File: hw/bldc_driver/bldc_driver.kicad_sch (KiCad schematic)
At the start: 25 parts, among them U1 CH32V30xRxTx, U14 SN65HVD230, U8 TPS54202DDC

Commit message: feat: add CNCs
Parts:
- removed R2: 300 ohm, Resistor_SMD:R_0603_1608Metric_Pad0.98x0.95mm_HandSolder, symbol #inventree:RC0603FR-07300RL
- added D15, D16, D17: KT-0603W, LED_SMD:LED_0603_1608Metric_Pad1.05x0.95mm_HandSolder, symbol Device:LED
- added J1: 430450412, Connector_Molex:Molex_Micro-Fit_3.0_43045-0412_2x02_P3.00mm_Vertical, symbol Connector_Generic:Conn_02x02_Odd_Even
- added J2: B4B-EH-A(LF)(SN), Connector_JST:JST_EH_B4B-EH-A_1x04_P2.50mm_Vertical, symbol Connector_Generic:Conn_01x04
- added J4: 1733583, TerminalBlock_Phoenix:TerminalBlock_Phoenix_MKDS-1,5-3-5.08_1x03_P5.08mm_Horizontal, symbol Connector:Screw_Terminal_01x03
- added R2, R36, R37, R6: 100 Ohm, Resistor_SMD:R_0603_1608Metric_Pad0.98x0.95mm_HandSolder, symbol Device:R
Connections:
- net +3V3: now also J2.4 (Pin_4)
- net +VDC: now also J1.1 (Pin_1)
- net GND: now also J2.1 (Pin_1), R2.1, R36.2, R37.2, R6.2
- net GNDPWR: now also J1.3 (Pin_3)
- net Motor/MOTOR_U: now also J4.1 (Pin_1)
- net Motor/MOTOR_V: now also J4.2 (Pin_2)
- net Motor/MOTOR_W: now also J4.3 (Pin_3)
- net Motor/PH_U_HI: now also U1.37 (PC6)
- net Motor/PH_U_LO: now also U1.38 (PC7)
- net Motor/PH_V_HI: now also U1.39 (PC8)
- net Motor/PH_V_LO: now also U1.40 (PC9)
- net Motor/PH_W_HI: now also U1.51 (PC10)
- net Motor/PH_W_LO: now also U1.52 (PC11)
- net Motor/SHUNT_CURR_P: now also U1.11 (PC3)
- net Motor/U_ADC_P: now also U1.8 (PC0)
- net Motor/V_ADC_P: now also U1.9 (PC1)
- net Motor/W_ADC_P: now also U1.10 (PC2)
- net at U1.34 (PB13): now also D15.2 (A)
- net at U1.35 (PB14): now also D16.2 (A)
- net at U1.36 (PB15): now also D17.2 (A)
- net at U1.46 (SWDIO): now also J2.3 (Pin_3)
- net at U1.49 (SWCLK): now also J2.2 (Pin_2)
- net at D1.1 (K): now also R2.2
- net CAN_L: now reaches U14.6 (CANL)
- net CAN_L: now also J1.4 (Pin_4)
- net CAN_H: now reaches U14.7 (CANH)
- net CAN_H: now also J1.2 (Pin_2)
- new net: D17.1 (K), R37.1
- new net: D15.1 (K), R6.1
- new net: D16.1 (K), R36.1
- no-connect marks 0 -> 6
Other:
- moved on the sheet: C1, C2, C3, C39, C4, C5, C6, C7, C8, C9, D1, D2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

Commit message: feat: start PCB
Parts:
- added F1: BSMD1206C-2200T, Fuse:Fuse_1206_3216Metric_Pad1.42x1.75mm_HandSolder, symbol Device:Fuse
- added J3: B4B-EH-A(LF)(SN), Connector_JST:JST_EH_B4B-EH-A_1x04_P2.50mm_Vertical, symbol Connector_Generic:Conn_01x04
- added TP6, TP7, TP8, TP9: TestPoint_Flag, TestPoint:TestPoint_Plated_Hole_D2.0mm, symbol Connector:TestPoint_Flag
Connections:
- net +3V3: now also J3.4 (Pin_4)
- net +VDC: now also F1.1; no longer J1.1 (Pin_1)
- net GND: now also J3.1 (Pin_1)
- net Motor/MOTOR_U: now also TP9.1
- net Motor/MOTOR_V: now also TP8.1
- net Motor/MOTOR_W: now also TP7.1
- net USART3_TX: now reaches U1.29 (PB10)
- net USART3_TX: now also J3.3 (Pin_3)
- net USART3_RX: now reaches U1.30 (PB11)
- net USART3_RX: now also J3.2 (Pin_2)
- new net: F1.2, J1.1 (Pin_1), TP6.1
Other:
- moved on the sheet: D1, J2, R2

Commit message: bldc: start placement
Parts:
- added C40: 0.1 µF, Capacitor_SMD:C_0805_2012Metric_Pad1.18x1.45mm_HandSolder, symbol #inventree:CL21B104KBCNNNC
- added C41, C42: 10 pF, Capacitor_SMD:C_0805_2012Metric_Pad1.18x1.45mm_HandSolder, symbol #inventree:CL21C100CBANNNC
- added R38, R39, R40: 4.7 kohm, Resistor_SMD:R_0603_1608Metric_Pad0.98x0.95mm_HandSolder, symbol #inventree:RC0603FR-074K7L
- added Y1: Crystal_GND24, Crystal:Crystal_SMD_3225-4Pin_3.2x2.5mm_HandSoldering, symbol Device:Crystal_GND24
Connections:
- net +3V3: now also R38.1, R39.1
- net GND: now also C40.2, C41.2, C42.2, R40.2, Y1.2, Y1.4
- net Motor/MOTOR_U: now also J4.3 (Pin_3); no longer J4.1 (Pin_1)
- net Motor/MOTOR_W: now also J4.1 (Pin_1); no longer J4.3 (Pin_3)
- net SWDIO: now reaches J2.3 (Pin_3), U1.46 (SWDIO)
- net SWCLK: now reaches J2.2 (Pin_2), U1.49 (SWCLK)
- net at U1.5 (OSC_IN): now also C41.1, Y1.3
- net at U1.6 (OSC_OUT): now also C42.1, Y1.1
- net at U1.60 (BOOT0): now also R39.2, R40.1
- net at U1.7 (~{RST}): now also C40.1, R38.2
- no-connect marks 6 -> 35
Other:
- note added: "RST BTN"
- moved on the sheet: C1, C2, C3, C4, C8, C9, R1, U1

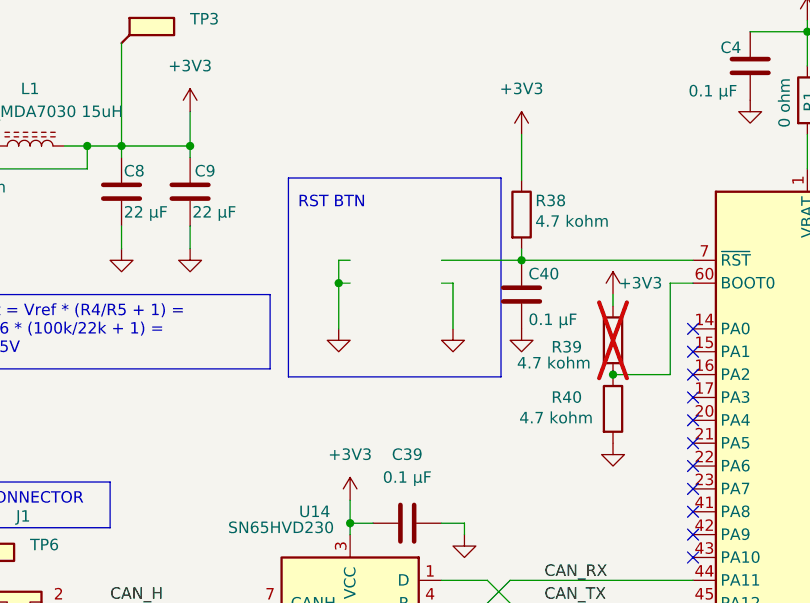
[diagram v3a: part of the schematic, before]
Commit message: bldc: placement mostly done
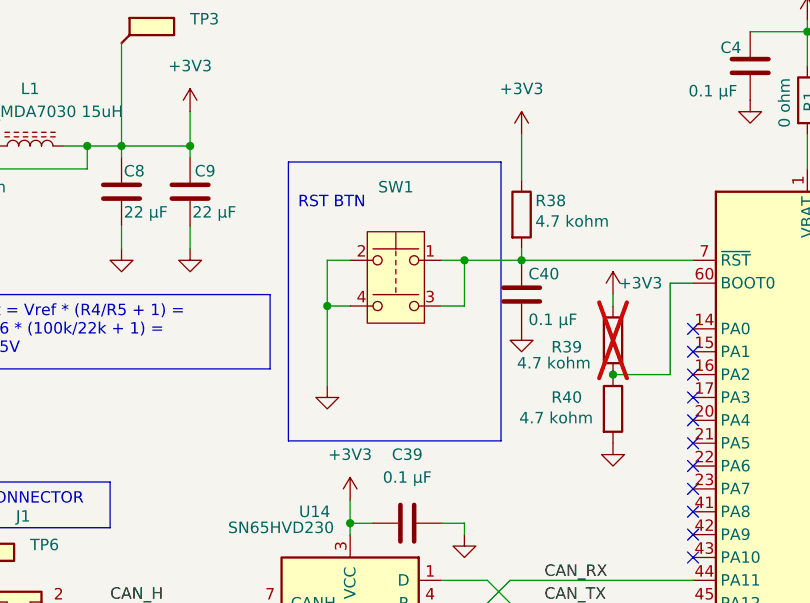
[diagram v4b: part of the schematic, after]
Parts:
- added SW1: BTSA-N-P-1, Button_Switch_THT:SW_PUSH_6mm_H8mm, symbol Switch:SW_Push_Dual
- R3: footprint Resistor_SMD:R_0201_0603Metric_Pad0.64x0.40mm_HandSolder -> Resistor_SMD:R_0603_1608Metric_Pad0.98x0.95mm_HandSolder
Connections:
- net GND: now also SW1.2, SW1.4
- net at C40.1, R38.2, U1.7 (~{RST}): now also SW1.1, SW1.3

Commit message: before reroute
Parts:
- removed C1, C2, C3, C4: 0.1 µF, Capacitor_SMD:C_0805_2012Metric_Pad1.18x1.45mm_HandSolder, symbol #inventree:CL21B104KBCNNNC
- removed U1: CH32V30xRxTx, Package_QFP:LQFP-64_10x10mm_P0.5mm, symbol MCU_WCH_CH32V3:CH32V30xRxTx
- added C55: 10 µF, Capacitor_SMD:C_0805_2012Metric_Pad1.18x1.45mm_HandSolder, symbol #inventree:CL21A106KOQNNNE
- added C56, C57, C58, C60: 0.1 µF, Capacitor_SMD:C_0805_2012Metric_Pad1.18x1.45mm_HandSolder, symbol #inventree:CL21B104KBCNNNC
- added C59: 1 µF, Capacitor_SMD:C_0805_2012Metric_Pad1.18x1.45mm_HandSolder, symbol #inventree:CL21B104KBCNNNC
- added C61: 10 nF, Capacitor_SMD:C_0805_2012Metric_Pad1.18x1.45mm_HandSolder, symbol #inventree:CL21B104KBCNNNC
- added R41, R42, R43, R44: 0 ohm, Resistor_SMD:R_0603_1608Metric_Pad0.98x0.95mm_HandSolder, symbol #inventree:RC0603FR-070RL
- added U15: STM32L431CCTx, Package_QFP:LQFP-48_7x7mm_P0.5mm, symbol MCU_ST_STM32L4:STM32L431CCTx
- added U16, U17: SN74LVC1G125DBV, Package_TO_SOT_SMD:SOT-23-5_HandSoldering, symbol 74xGxx:SN74LVC1G125DBV
- J2: value B4B-EH-A(LF)(SN) -> B6B-EH-A(LF)(SN); footprint Connector_JST:JST_EH_B4B-EH-A_1x04_P2.50mm_Vertical -> Connector_JST:JST_EH_B6B-EH-A_1x06_P2.50mm_Vertical; symbol Connector_Generic:Conn_01x04 -> Connector_Generic:Conn_01x06
- R4: footprint Resistor_SMD:R_0201_0603Metric_Pad0.64x0.40mm_HandSolder -> Resistor_SMD:R_0603_1608Metric_Pad0.98x0.95mm_HandSolder
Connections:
- net +3V3: now also J2.6 (Pin_6), C55.1, C56.2, C57.2, C58.2, C59.2, C60.2, C61.2, U15.24 (VDD), U15.36 (VDD), U15.48 (VDD), U15.9 (VDDA), U16.5 (VCC), U17.5 (VCC); no longer J2.4 (Pin_4)
- net CAN_RX: now also U14.1 (D), R42.1; no longer U14.4 (R)
- net CAN_TX: now also U14.4 (R), R41.2; no longer U14.1 (D)
- net GND: now also C41.1, C42.1, C55.2, C56.1, C57.1, C58.1, C59.1, C60.1, C61.1, U15.23 (VSS), U15.35 (VSS), U15.47 (VSS), U15.8 (VSSA), U16.1, U16.3 (GND), U17.1, U17.3 (GND); no longer C41.2, C42.2
- net Motor/MOTOR_U: now also TP7.1; no longer TP9.1
- net Motor/MOTOR_W: now also TP9.1; no longer TP7.1
- net SWCLK: now also J2.3 (Pin_3), U15.37 (PA14); no longer J2.2 (Pin_2)
- net SWDIO: now also J2.4 (Pin_4), U15.34 (PA13); no longer J2.3 (Pin_3)
- net at R1.2: now also U15.1 (VBAT)
- net at D15.2 (A): now also U15.38 (PA15)
- net at D16.2 (A): now also U15.39 (PB3)
- net at D17.2 (A): now also U15.22 (PB11)
- net at Y1.3: now also C41.2, U15.5 (PH0); no longer C41.1
- net at Y1.1: now also C42.2, U15.6 (PH1); no longer C42.1
- net at R39.2, R40.1: now also U15.44 (PH3)
- net NRESET: now reaches C40.1, R38.2, SW1.1, SW1.3
- net NRESET: now also R44.2, U15.7 (NRST)
- net USART3_RX renamed USART1_RX
- net USART1_RX: now also U16.2
- net USART3_TX renamed USART1_TX
- net USART1_TX: now also U17.4
- new net: J2.2 (Pin_2), R43.1
- new net: U15.43 (PB7), U16.4
- new net: R42.2, U15.33 (PA12)
- new net: R41.1, U15.32 (PA11)
- new net: J2.5 (Pin_5), R44.1
- new net: U15.42 (PB6), U17.2
- new net PH_U_HI: U15.29 (PA8)
- new net PH_U_LO: U15.26 (PB13)
- new net PH_V_HI: U15.30 (PA9)
- new net PH_V_LO: U15.27 (PB14)
- new net PH_W_HI: U15.31 (PA10)
- new net PH_W_LO: U15.28 (PB15)
- new net SHUNT_CURR_N: U15.17 (PA7)
- new net SHUNT_CURR_P: U15.16 (PA6)
- new net U_ADC_N: U15.11 (PA1)
- new net U_ADC_P: U15.10 (PA0)
- new net V_ADC_N: U15.13 (PA3)
- new net V_ADC_P: U15.12 (PA2)
- new net W_ADC_N: U15.15 (PA5)
- new net W_ADC_P: U15.14 (PA4)
- no-connect marks 35 -> 14
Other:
- note added: "ADC1"
- moved on the sheet: C39, C40, C41, C42, D15, D16, D17, F1, J1, J3, J4, R1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

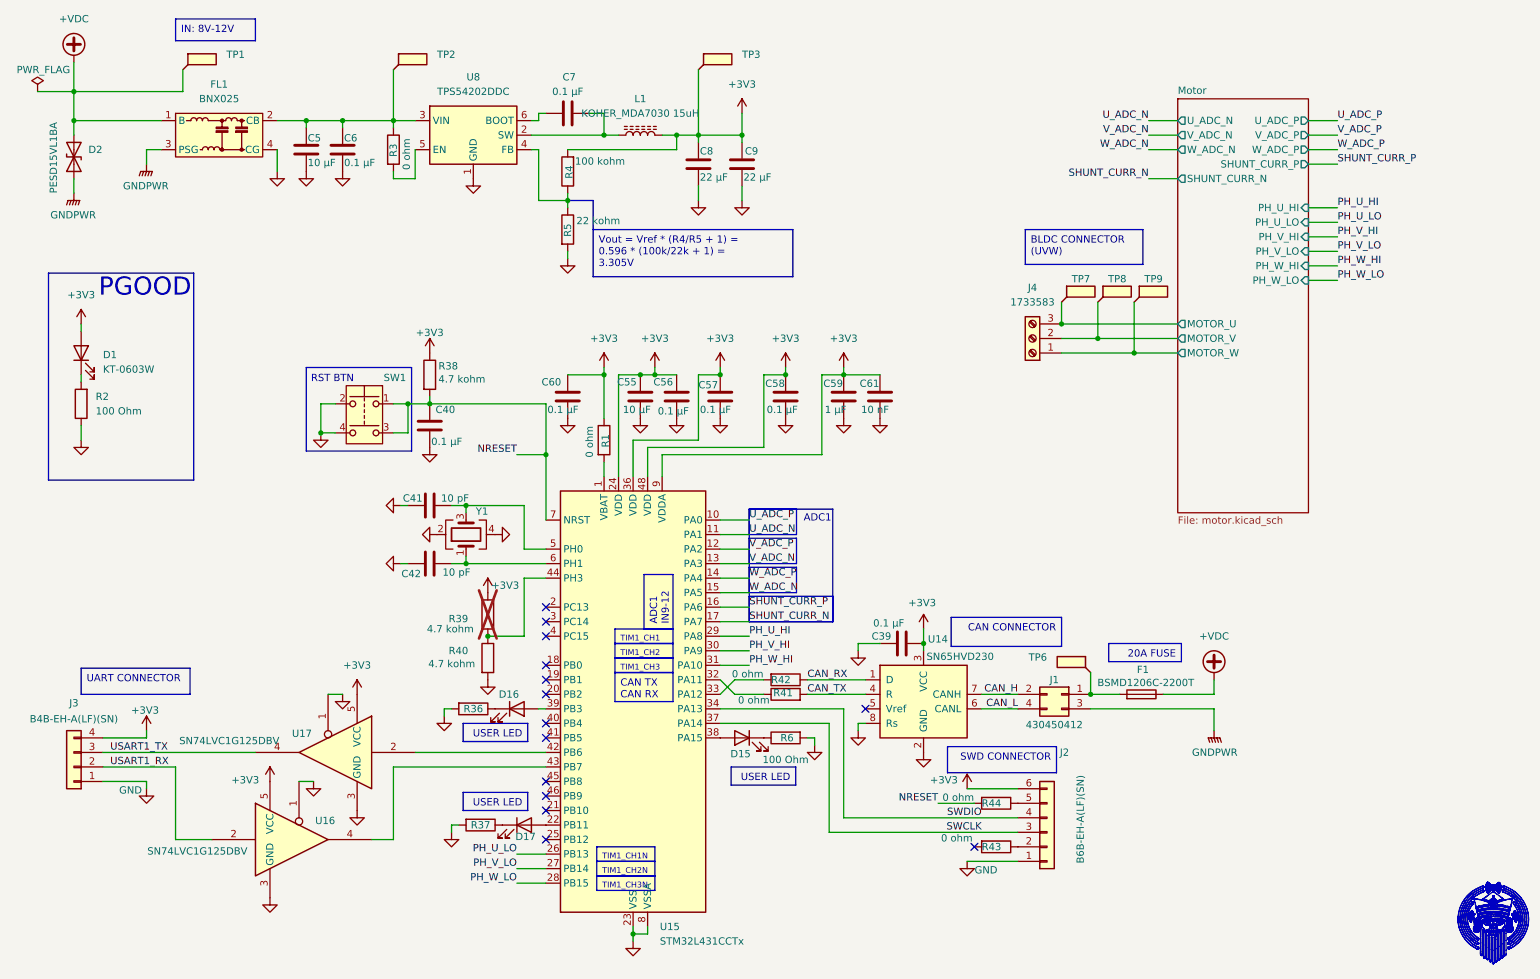
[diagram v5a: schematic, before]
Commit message: half routed
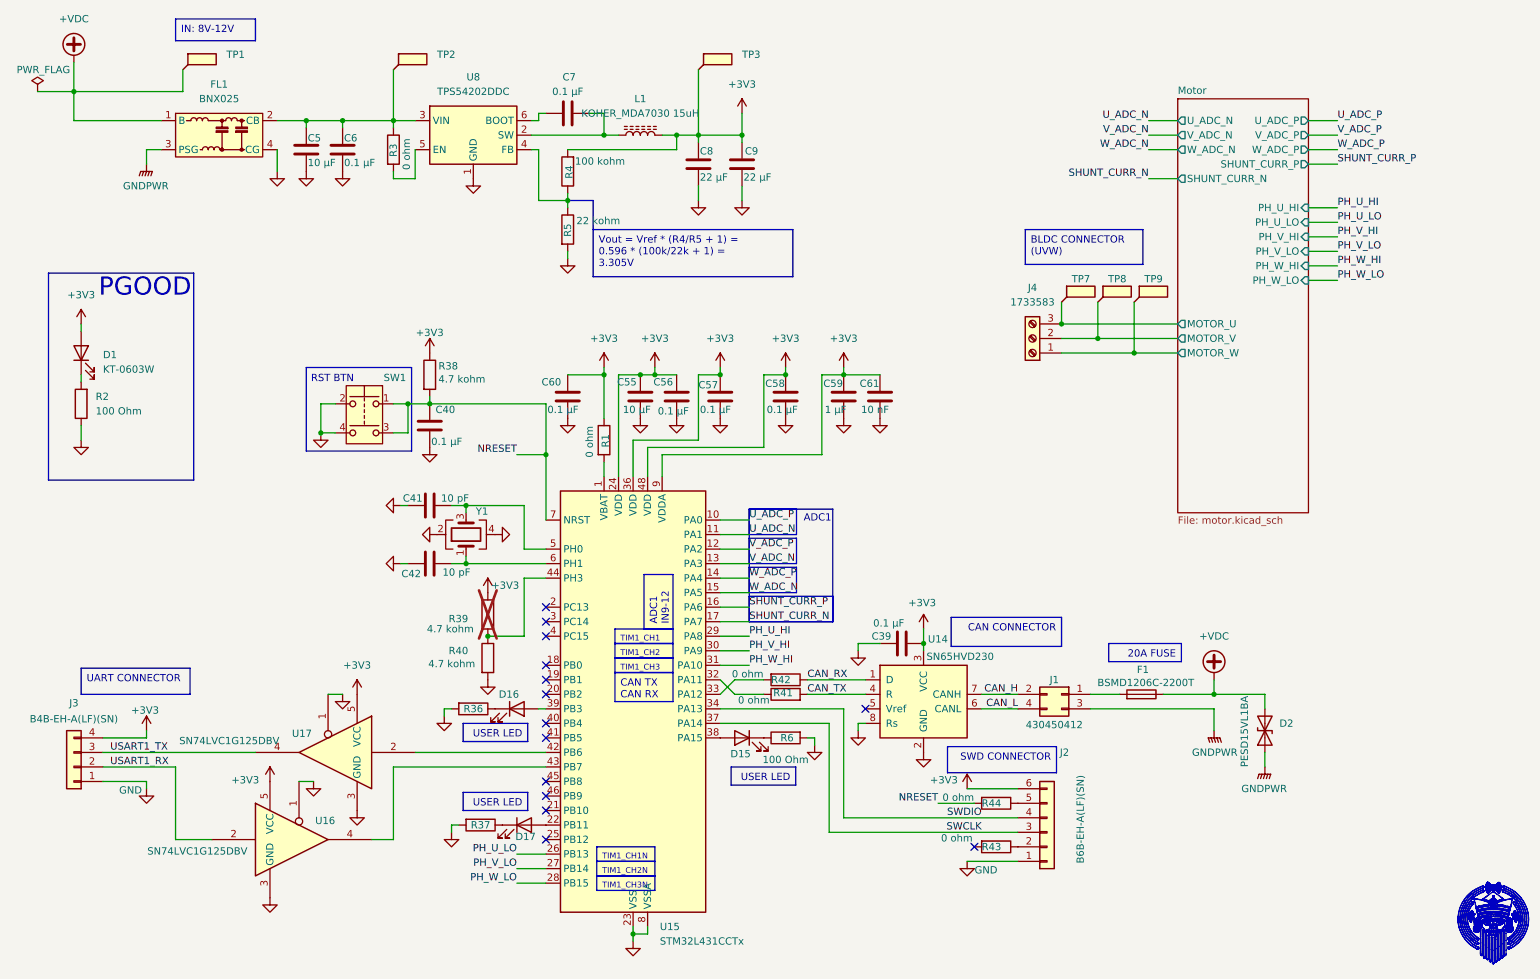
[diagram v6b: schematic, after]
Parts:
- removed TP6: TestPoint_Flag, TestPoint:TestPoint_Plated_Hole_D2.0mm, symbol Connector:TestPoint_Flag
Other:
- moved on the sheet: D2
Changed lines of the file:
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@@
 	)
 	(junction
-		(at 29.21 33.02)
-		(diameter 0)
-		(color 0 0 0 0)
-	)
-	(junction
 		(at 101.6 123.19)
 		(diameter 0)
@@
 	)
 	(junction
-		(at 207.01 133.35)
-		(diameter 0)
-		(color 0 0 0 0)
-	)
-	(junction
 		(at 128.27 77.47)
 		(diameter 0)
@@
 	)
 	(junction
+		(at 228.6 133.35)
+		(diameter 0)
+		(color 0 0 0 0)
+	)
+	(junction
 		(at 97.79 110.49)
 		(diameter 0)
@@
 	(wire
 		(pts
+			(xy 237.49 143.51) (xy 237.49 146.05)
+		)
+		(stroke
+			(width 0)
+			(type default)
+		)
+	)
+	(wire
+		(pts
 			(xy 29.21 27.94) (xy 29.21 33.02)
 		)
@@
 	(wire
 		(pts
+			(xy 237.49 133.35) (xy 237.49 135.89)
+		)
+		(stroke
+			(width 0)
+			(type default)
+		)
+	)
+	(wire
+		(pts
 			(xy 46.99 146.05) (xy 46.99 158.75)
 		)
@@
 	(wire
 		(pts
-			(xy 29.21 43.18) (xy 29.21 45.72)
-		)
-		(stroke
-			(width 0)
-			(type default)
-		)
-	)
-	(wire
-		(pts
 			(xy 95.25 135.89) (xy 93.98 135.89)
 		)
@@
 	(wire
 		(pts
-			(xy 207.01 129.54) (xy 207.01 133.35)
-		)
-		(stroke
-			(width 0)
-			(type default)
-		)
-	)
-	(wire
-		(pts
 			(xy 129.54 175.26) (xy 129.54 173.99)
 		)
@@
 	(wire
 		(pts
-			(xy 29.21 33.02) (xy 29.21 35.56)
-		)
-		(stroke
-			(width 0)
-			(type default)
-		)
-	)
-	(wire
-		(pts
 			(xy 119.38 31.75) (xy 121.92 31.75)
 		)
@@
 	(wire
 		(pts
+			(xy 228.6 133.35) (xy 237.49 133.35)
+		)
+		(stroke
+			(width 0)
+			(type default)
+		)
+	)
+	(wire
+		(pts
 			(xy 107.95 107.95) (xy 111.76 107.95)
 		)
@@
 	(symbol
 		(lib_id "power:GNDPWR")
-		(at 29.21 45.72 0)
+		(at 237.49 146.05 0)
 		(unit 1)
 		(exclude_from_sim no)
@@
 		(fields_autoplaced yes)
 		(property "Reference" "#PWR022"
-			(at 29.21 50.8 0)
+			(at 237.49 151.13 0)
 			(effects
 				(font
@@
 		)
 		(property "Value" "GNDPWR"
-			(at 29.083 49.53 0)
+			(at 237.363 149.86 0)
 			(effects
 				(font
@@
 		)
 		(property "Footprint" ""
-			(at 29.21 46.99 0)
+			(at 237.49 147.32 0)
 			(effects
 				(font
@@
 		)
 		(property "Datasheet" ""
-			(at 29.21 46.99 0)
+			(at 237.49 147.32 0)
 			(effects
 				(font
@@
 		)
 		(property "Description" "Power symbol creates a global label with name \"GNDPWR\" , global ground"
-			(at 29.21 45.72 0)
+			(at 237.49 146.05 0)
 			(effects
 				(font
@@
 	(symbol
 		(lib_id "Device:D_TVS")
-		(at 29.21 39.37 90)
+		(at 237.49 139.7 90)
 		(unit 1)
 		(exclude_from_sim no)
@@
 		(dnp no)
 		(property "Reference" "D2"
-			(at 31.75 38.0999 90)
+			(at 240.03 138.4299 90)
 			(effects
 				(font
@@
 		)
 		(property "Value" "PESD15VL1BA"
-			(at 25.654 33.274 0)
+			(at 233.934 133.604 0)
 			(effects
 				(font
@@
 		)
 		(property "Footprint" "Diode_SMD:D_SOD-323_HandSoldering"
-			(at 29.21 39.37 0)
+			(at 237.49 139.7 0)
 			(effects
 				(font
@@
 		)
 		(property "Datasheet" "~"
-			(at 29.21 39.37 0)
+			(at 237.49 139.7 0)
 			(effects
 				(font
@@
 		)
 		(property "Description" "Bidirectional transient-voltage-suppression diode"
-			(at 29.21 39.37 0)
+			(at 237.49 139.7 0)
 			(effects
 				(font
@@
 		)
 		(instances
-			(project ""
+			(project "bldc_driver"
 				(path "/6f0070f8-99b2-4a48-98f9-774d985c191f"
 					(reference "D2")
@@
 					(unit 1)
 				)
-			)
-		)
-	)
-	(symbol
-		(lib_id "Connector:TestPoint_Flag")
-		(at 207.01 129.54 0)
-		(mirror y)
-		(unit 1)
-		(exclude_from_sim no)
-		(in_bom yes)
-		(on_board yes)
-		(dnp no)
-		(property "Reference" "TP6"
-			(at 199.39 126.8729 0)
-			(effects
-				(font
-					(size 1.27 1.27)
-				)
-				(justify left)
-			)
-		)
-		(property "Value" "TestPoint_Flag"
-			(at 206.248 124.714 0)
-			(effects
-				(font
-					(size 1.27 1.27)
-				)
-				(justify left)
-				(hide yes)
-			)
-		)
-		(property "Footprint" "TestPoint:TestPoint_Plated_Hole_D2.0mm"
-			(at 201.93 129.54 0)
-			(effects
-				(font
-					(size 1.27 1.27)
-				)
-				(hide yes)
-			)
-		)
-		(property "Datasheet" "~"
-			(at 201.93 129.54 0)
-			(effects
-				(font
-					(size 1.27 1.27)
-				)
-				(hide yes)
-			)
-		)
-		(property "Description" "test point (alternative flag-style design)"
-			(at 207.01 129.54 0)
-			(effects
-				(font
-					(size 1.27 1.27)
-				)
-				(hide yes)
-			)
-		)
-		(pin "1"
-		)
-		(instances
-			(project "bldc_driver"
-				(path "/6f0070f8-99b2-4a48-98f9-774d985c191f"
-					(reference "TP6")
-					(unit 1)
-				)

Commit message: full route
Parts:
- removed R1: 0 ohm, Resistor_SMD:R_0603_1608Metric_Pad0.98x0.95mm_HandSolder, symbol #inventree:RC0603FR-070RL
- added C62, C63: 0.1 µF, Capacitor_SMD:C_0805_2012Metric_Pad1.18x1.45mm_HandSolder, symbol #inventree:CL21B104KBCNNNC
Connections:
- net +3V3: now also U15.1 (VBAT), C62.2, C63.1
- net +VDC: no longer D2.2 (A2)
- net GND: now also C62.1, C63.2
- net at F1.2, J1.1 (Pin_1): now also D2.2 (A2)
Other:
- moved on the sheet: D2, F1
